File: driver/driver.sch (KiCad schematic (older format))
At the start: 13 parts, among them J1 BARREL_JACK, U1 MCP23017, U2 Teensy3.2, U3 MCP23017, U4 LM7815CT, U5 MCP23017, U6 LF50ABDT-TR, U7 MCP23017, U8 MCP23017, U9 MCP23017

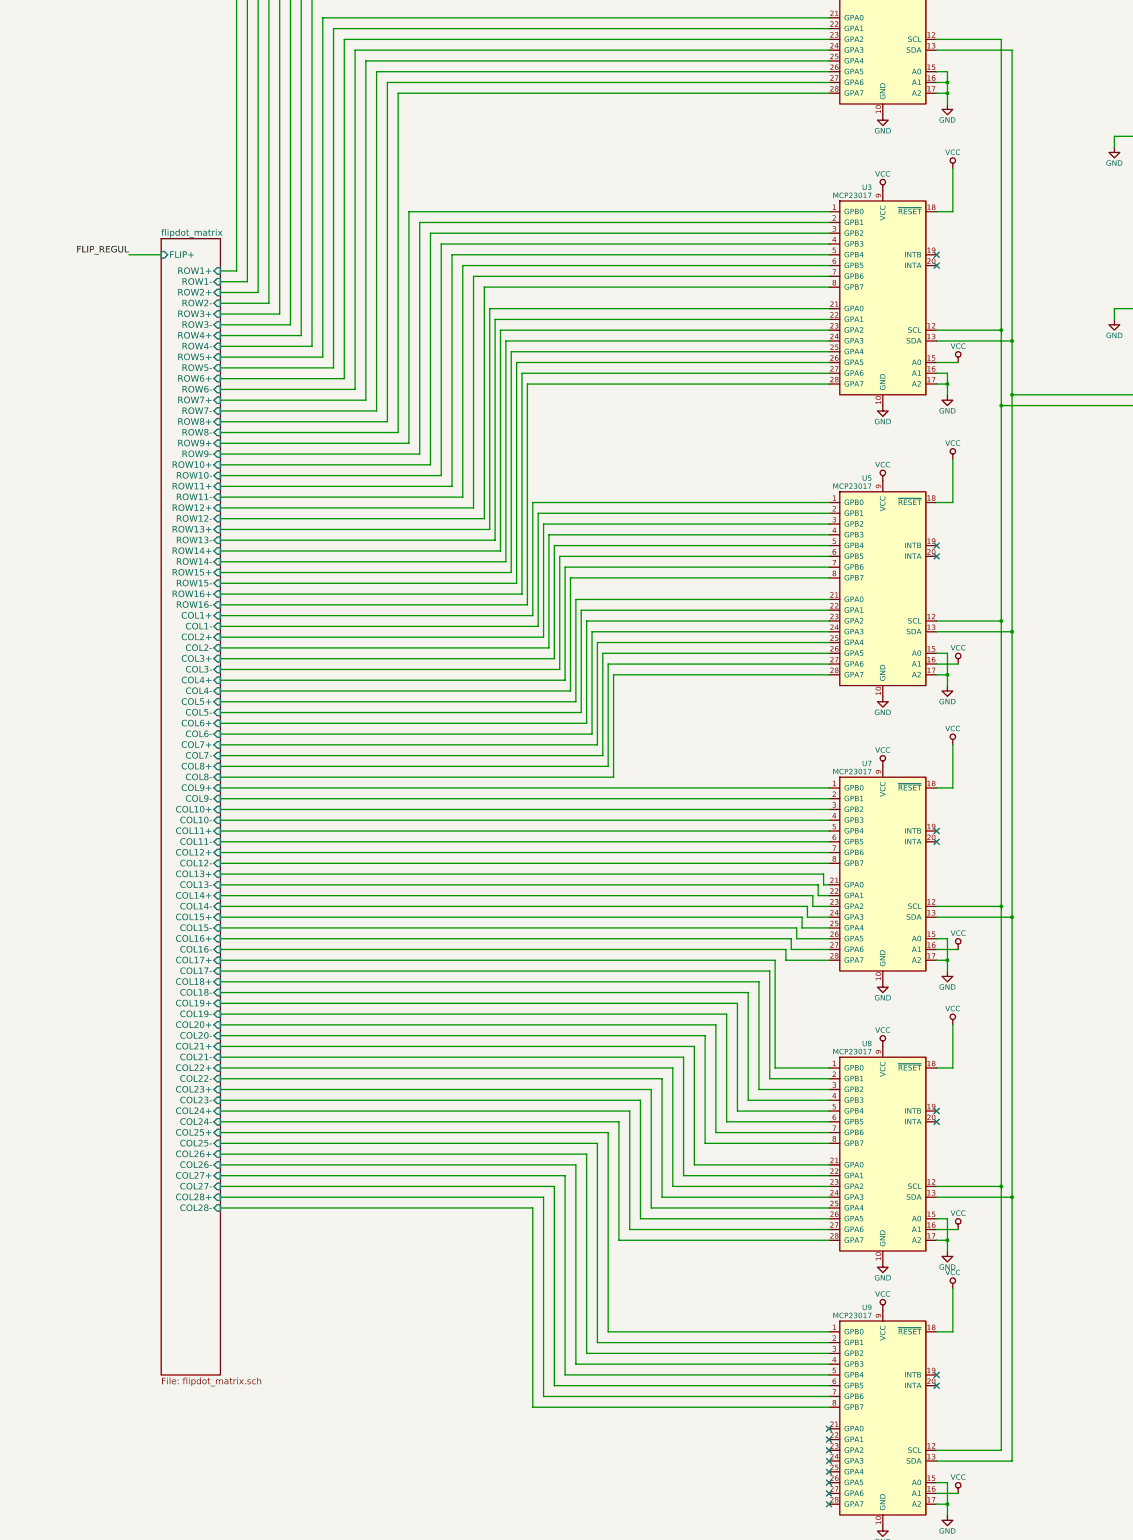
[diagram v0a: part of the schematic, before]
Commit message: Better row pins
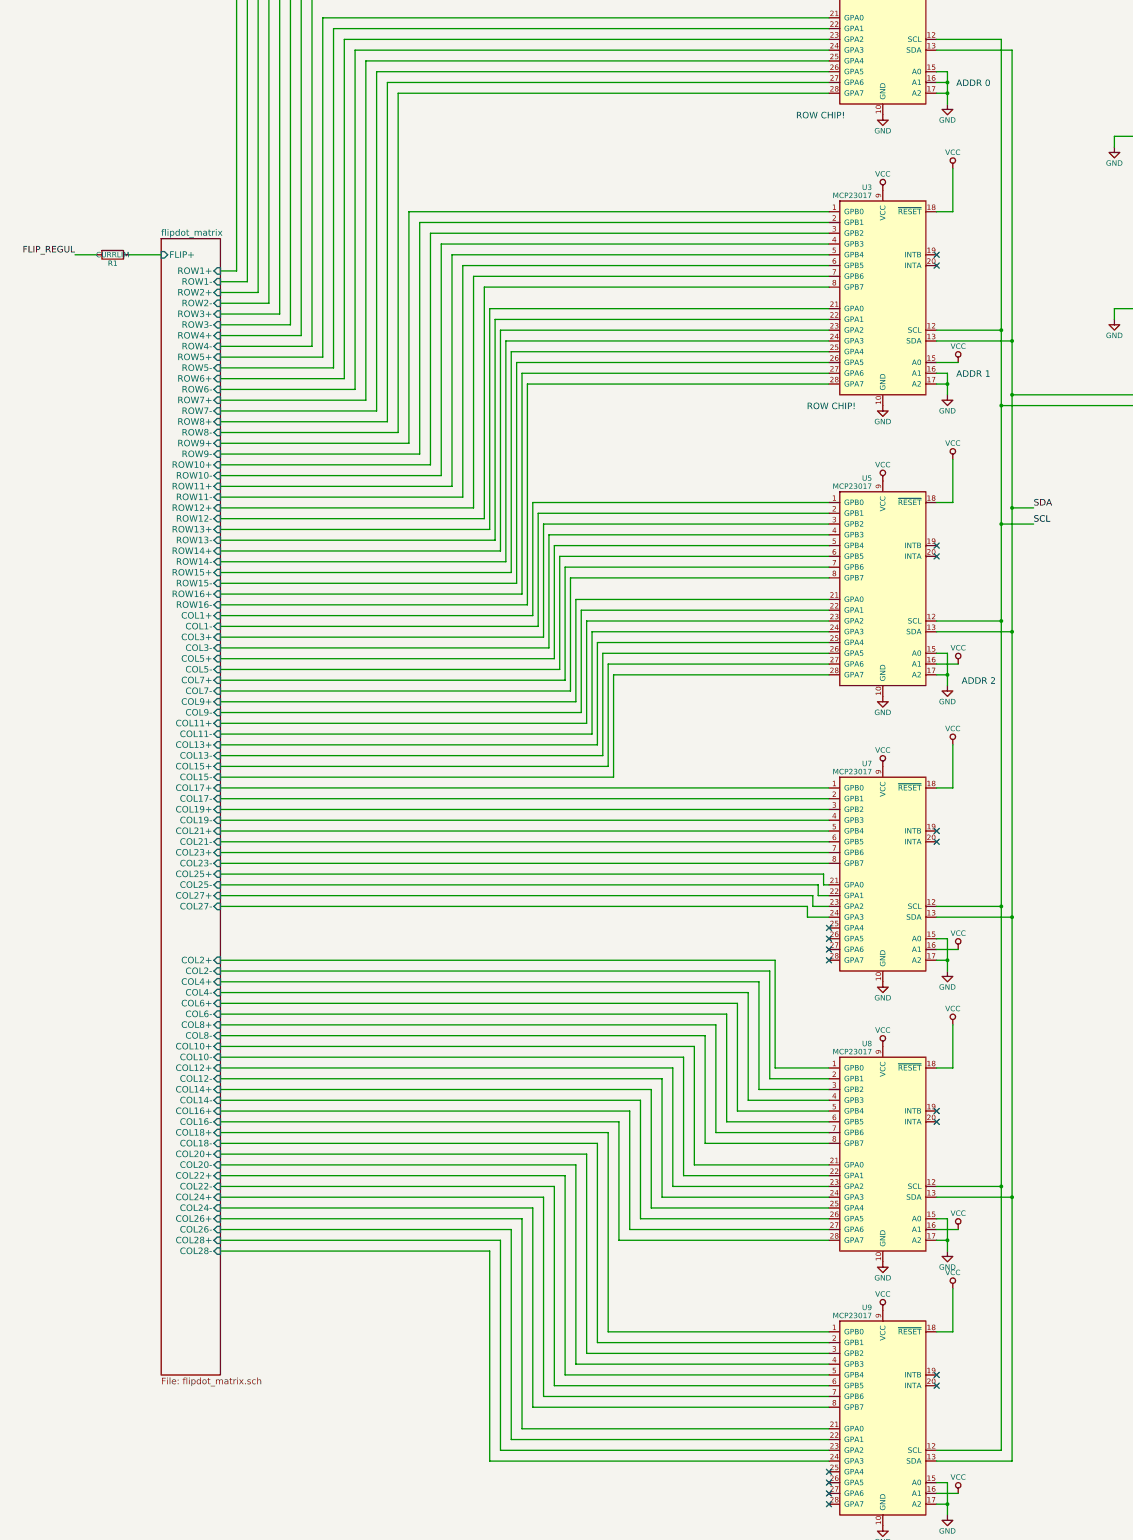
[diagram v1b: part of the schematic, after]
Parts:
- added R1: CURRLIM, symbol R
- C1, C2, C3: footprint (none) -> Capacitors_THT:CP_Radial_Tantal_D10.5mm_P5.00mm
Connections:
- net FLIP_REGUL: now also R1.2
- net flipdot_matrix/COL10+: now also U8.21 (GPA0); no longer U7.3 (GPB2)
- net flipdot_matrix/COL10-: now also U8.22 (GPA1); no longer U7.4 (GPB3)
- net flipdot_matrix/COL11+: now also U5.23 (GPA2); no longer U7.5 (GPB4)
- net flipdot_matrix/COL11-: now also U5.24 (GPA3); no longer U7.6 (GPB5)
- net flipdot_matrix/COL12+: now also U8.23 (GPA2); no longer U7.7 (GPB6)
- net flipdot_matrix/COL12-: now also U8.24 (GPA3); no longer U7.8 (GPB7)
- net flipdot_matrix/COL13+: now also U5.25 (GPA4); no longer U7.21 (GPA0)
- net flipdot_matrix/COL13-: now also U5.26 (GPA5); no longer U7.22 (GPA1)
- net flipdot_matrix/COL14+: now also U8.25 (GPA4); no longer U7.23 (GPA2)
- net flipdot_matrix/COL14-: now also U8.26 (GPA5); no longer U7.24 (GPA3)
- net flipdot_matrix/COL15+: now also U5.27 (GPA6); no longer U7.25 (GPA4)
- net flipdot_matrix/COL15-: now also U5.28 (GPA7); no longer U7.26 (GPA5)
- net flipdot_matrix/COL16+: now also U8.27 (GPA6); no longer U7.27 (GPA6)
- net flipdot_matrix/COL16-: now also U8.28 (GPA7); no longer U7.28 (GPA7)
- net flipdot_matrix/COL17+: now also U7.1 (GPB0); no longer U8.1 (GPB0)
- net flipdot_matrix/COL17-: now also U7.2 (GPB1); no longer U8.2 (GPB1)
- net flipdot_matrix/COL18+: now also U9.1 (GPB0); no longer U8.3 (GPB2)
- net flipdot_matrix/COL18-: now also U9.2 (GPB1); no longer U8.4 (GPB3)
- net flipdot_matrix/COL19+: now also U7.3 (GPB2); no longer U8.5 (GPB4)
- net flipdot_matrix/COL19-: now also U7.4 (GPB3); no longer U8.6 (GPB5)
- net flipdot_matrix/COL2+: now also U8.1 (GPB0); no longer U5.3 (GPB2)
- net flipdot_matrix/COL2-: now also U8.2 (GPB1); no longer U5.4 (GPB3)
- net flipdot_matrix/COL20+: now also U9.3 (GPB2); no longer U8.7 (GPB6)
- net flipdot_matrix/COL20-: now also U9.4 (GPB3); no longer U8.8 (GPB7)
- net flipdot_matrix/COL21+: now also U7.5 (GPB4); no longer U8.21 (GPA0)
- net flipdot_matrix/COL21-: now also U7.6 (GPB5); no longer U8.22 (GPA1)
- net flipdot_matrix/COL22+: now also U9.5 (GPB4); no longer U8.23 (GPA2)
- net flipdot_matrix/COL22-: now also U9.6 (GPB5); no longer U8.24 (GPA3)
- net flipdot_matrix/COL23+: now also U7.7 (GPB6); no longer U8.25 (GPA4)
- net flipdot_matrix/COL23-: now also U7.8 (GPB7); no longer U8.26 (GPA5)
- net flipdot_matrix/COL24+: now also U9.7 (GPB6); no longer U8.27 (GPA6)
- net flipdot_matrix/COL24-: now also U9.8 (GPB7); no longer U8.28 (GPA7)
- net flipdot_matrix/COL25+: now also U7.21 (GPA0); no longer U9.1 (GPB0)
- net flipdot_matrix/COL25-: now also U7.22 (GPA1); no longer U9.2 (GPB1)
- net flipdot_matrix/COL26+: now also U9.21 (GPA0); no longer U9.3 (GPB2)
- net flipdot_matrix/COL26-: now also U9.22 (GPA1); no longer U9.4 (GPB3)
- net flipdot_matrix/COL27+: now also U7.23 (GPA2); no longer U9.5 (GPB4)
- net flipdot_matrix/COL27-: now also U7.24 (GPA3); no longer U9.6 (GPB5)
- net flipdot_matrix/COL28+: now also U9.23 (GPA2); no longer U9.7 (GPB6)
- net flipdot_matrix/COL28-: now also U9.24 (GPA3); no longer U9.8 (GPB7)
- net flipdot_matrix/COL3+: now also U5.3 (GPB2); no longer U5.5 (GPB4)
- net flipdot_matrix/COL3-: now also U5.4 (GPB3); no longer U5.6 (GPB5)
- net flipdot_matrix/COL4+: now also U8.3 (GPB2); no longer U5.7 (GPB6)
- net flipdot_matrix/COL4-: now also U8.4 (GPB3); no longer U5.8 (GPB7)
- net flipdot_matrix/COL5+: now also U5.5 (GPB4); no longer U5.21 (GPA0)
- net flipdot_matrix/COL5-: now also U5.6 (GPB5); no longer U5.22 (GPA1)
- net flipdot_matrix/COL6+: now also U8.5 (GPB4); no longer U5.23 (GPA2)
- net flipdot_matrix/COL6-: now also U8.6 (GPB5); no longer U5.24 (GPA3)
- net flipdot_matrix/COL7+: now also U5.7 (GPB6); no longer U5.25 (GPA4)
- net flipdot_matrix/COL7-: now also U5.8 (GPB7); no longer U5.26 (GPA5)
- net flipdot_matrix/COL8+: now also U8.7 (GPB6); no longer U5.27 (GPA6)
- net flipdot_matrix/COL8-: now also U8.8 (GPB7); no longer U5.28 (GPA7)
- net flipdot_matrix/COL9+: now also U5.21 (GPA0); no longer U7.1 (GPB0)
- net flipdot_matrix/COL9-: now also U5.22 (GPA1); no longer U7.2 (GPB1)
- net SCL: now reaches U1.12 (SCL), U2.26 (19_A5_SCL0_Touch), U3.12 (SCL), U5.12 (SCL), U7.12 (SCL), U8.12 (SCL), U9.12 (SCL)
- net SDA: now reaches U1.13 (SDA), U2.25 (18_A4_SDA0_Touch), U3.13 (SDA), U5.13 (SDA), U7.13 (SDA), U8.13 (SDA), U9.13 (SDA)
- new net flipdot_matrix/FLIP+: R1.1
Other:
- note added: "ADDR 0\n"
- note added: "ADDR 1"
- note added: "ADDR 2"
- note added: "ROW CHIP!"
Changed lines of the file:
@@
 F35 "COL1+" I R 8050 7600 60
 F36 "COL1-" I R 8050 7700 60
-F37 "COL2+" I R 8050 7800 60
-F38 "COL2-" I R 8050 7900 60
-F39 "COL3+" I R 8050 8000 60
-F40 "COL4+" I R 8050 8200 60
-F41 "COL3-" I R 8050 8100 60
-F42 "COL4-" I R 8050 8300 60
-F43 "COL5-" I R 8050 8500 60
-F44 "COL5+" I R 8050 8400 60
-F45 "COL6+" I R 8050 8600 60
-F46 "COL6-" I R 8050 8700 60
-F47 "COL7-" I R 8050 8900 60
-F48 "COL7+" I R 8050 8800 60
-F49 "COL8-" I R 8050 9100 60
-F50 "COL8+" I R 8050 9000 60
-F51 "COL9+" I R 8050 9200 60
-F52 "COL9-" I R 8050 9300 60
-F53 "COL10-" I R 8050 9500 60
-F54 "COL11-" I R 8050 9700 60
-F55 "COL10+" I R 8050 9400 60
-F56 "COL11+" I R 8050 9600 60
-F57 "COL12+" I R 8050 9800 60
-F58 "COL12-" I R 8050 9900 60
-F59 "COL13+" I R 8050 10000 60
-F60 "COL14+" I R 8050 10200 60
-F61 "COL13-" I R 8050 10100 60
-F62 "COL14-" I R 8050 10300 60
-F63 "COL15+" I R 8050 10400 60
-F64 "COL15-" I R 8050 10500 60
-F65 "COL16+" I R 8050 10600 60
-F66 "COL16-" I R 8050 10700 60
-F67 "COL17+" I R 8050 10800 60
-F68 "COL18+" I R 8050 11000 60
-F69 "COL17-" I R 8050 10900 60
-F70 "COL18-" I R 8050 11100 60
-F71 "COL19-" I R 8050 11300 60
-F72 "COL19+" I R 8050 11200 60
-F73 "COL20+" I R 8050 11400 60
-F74 "COL20-" I R 8050 11500 60
-F75 "COL21-" I R 8050 11700 60
-F76 "COL21+" I R 8050 11600 60
-F77 "COL22-" I R 8050 11900 60
-F78 "COL22+" I R 8050 11800 60
-F79 "COL23+" I R 8050 12000 60
-F80 "COL23-" I R 8050 12100 60
-F81 "COL24-" I R 8050 12300 60
-F82 "COL25-" I R 8050 12500 60
-F83 "COL24+" I R 8050 12200 60
-F84 "COL25+" I R 8050 12400 60
-F85 "COL26+" I R 8050 12600 60
-F86 "COL26-" I R 8050 12700 60
-F87 "COL27+" I R 8050 12800 60
-F88 "COL28+" I R 8050 13000 60
-F89 "COL27-" I R 8050 12900 60
-F90 "COL28-" I R 8050 13100 60
+F37 "COL2+" I R 8050 10800 60
+F38 "COL2-" I R 8050 10900 60
+F39 "COL3+" I R 8050 7800 60
+F40 "COL4+" I R 8050 11000 60
+F41 "COL3-" I R 8050 7900 60
+F42 "COL4-" I R 8050 11100 60
+F43 "COL5-" I R 8050 8100 60
+F44 "COL5+" I R 8050 8000 60
+F45 "COL6+" I R 8050 11200 60
+F46 "COL6-" I R 8050 11300 60
+F47 "COL7-" I R 8050 8300 60
+F48 "COL7+" I R 8050 8200 60
+F49 "COL8-" I R 8050 11500 60
+F50 "COL8+" I R 8050 11400 60
+F51 "COL9+" I R 8050 8400 60
+F52 "COL9-" I R 8050 8500 60
+F53 "COL10-" I R 8050 11700 60
+F54 "COL11-" I R 8050 8700 60
+F55 "COL10+" I R 8050 11600 60
+F56 "COL11+" I R 8050 8600 60
+F57 "COL12+" I R 8050 11800 60
+F58 "COL12-" I R 8050 11900 60
+F59 "COL13+" I R 8050 8800 60
+F60 "COL14+" I R 8050 12000 60
+F61 "COL13-" I R 8050 8900 60
+F62 "COL14-" I R 8050 12100 60
+F63 "COL15+" I R 8050 9000 60
+F64 "COL15-" I R 8050 9100 60
+F65 "COL16+" I R 8050 12200 60
+F66 "COL16-" I R 8050 12300 60
+F67 "COL17+" I R 8050 9200 60
+F68 "COL18+" I R 8050 12400 60
+F69 "COL17-" I R 8050 9300 60
+F70 "COL18-" I R 8050 12500 60
+F71 "COL19-" I R 8050 9500 60
+F72 "COL19+" I R 8050 9400 60
+F73 "COL20+" I R 8050 12600 60
+F74 "COL20-" I R 8050 12700 60
+F75 "COL21-" I R 8050 9700 60
+F76 "COL21+" I R 8050 9600 60
+F77 "COL22-" I R 8050 12900 60
+F78 "COL22+" I R 8050 12800 60
+F79 "COL23+" I R 8050 9800 60
+F80 "COL23-" I R 8050 9900 60
+F81 "COL24-" I R 8050 13100 60
+F82 "COL25-" I R 8050 10100 60
+F83 "COL24+" I R 8050 13000 60
+F84 "COL25+" I R 8050 10000 60
+F85 "COL26+" I R 8050 13200 60
+F86 "COL26-" I R 8050 13300 60
+F87 "COL27+" I R 8050 10200 60
+F88 "COL28+" I R 8050 13400 60
+F89 "COL27-" I R 8050 10300 60
+F90 "COL28-" I R 8050 13500 60
 $EndSheet
 Wire Wire Line
@@
 	13500 10300 8050 10300
 Wire Wire Line
-	13700 10500 13450 10500
-Wire Wire Line
-	13450 10500 13450 10400
-Wire Wire Line
-	13450 10400 8050 10400
-Wire Wire Line
-	13700 10600 13400 10600
-Wire Wire Line
-	13400 10600 13400 10500
-Wire Wire Line
-	13400 10500 8050 10500
-Wire Wire Line
-	13700 10700 13350 10700
-Wire Wire Line
-	13350 10700 13350 10600
-Wire Wire Line
-	13350 10600 8050 10600
-Wire Wire Line
-	13700 10800 13300 10800
-Wire Wire Line
-	13300 10800 13300 10700
-Wire Wire Line
-	13300 10700 8050 10700
-Wire Wire Line
 	13700 11800 13200 11800
 Wire Wire Line
@@
 Wire Wire Line
 	8050 13100 10950 13100
-NoConn ~ 13700 15150
-NoConn ~ 13700 15250
-NoConn ~ 13700 15350
-NoConn ~ 13700 15450
 NoConn ~ 13700 15550
 NoConn ~ 13700 15650
@@
 Wire Wire Line
 	7500 4250 7200 4250
-Text Label 7200 4250 2    60   ~ 0
+Text Label 6700 4250 2    60   ~ 0
 FLIP_REGUL
 Wire Wire Line
@@
 F 0 "C1" H 19175 8000 50  0000 L CNN
 F 1 "10uF" H 19175 7800 50  0000 L CNN
-F 2 "" H 19188 7750 50  0001 C CNN
+F 2 "Capacitors_THT:CP_Radial_Tantal_D10.5mm_P5.00mm" H 19188 7750 50  0001 C CNN
 F 3 "" H 19150 7900 50  0001 C CNN
 	1    19150 7900
@@
 F 0 "C2" H 20575 8000 50  0000 L CNN
 F 1 "10uF" H 20575 7800 50  0000 L CNN
-F 2 "" H 20588 7750 50  0001 C CNN
+F 2 "Capacitors_THT:CP_Radial_Tantal_D10.5mm_P5.00mm" H 20588 7750 50  0001 C CNN
 F 3 "" H 20550 7900 50  0001 C CNN
 	1    20550 7900
@@
 F 0 "C3" H 19625 6750 50  0000 L CNN
 F 1 "10uF" H 19625 6550 50  0000 L CNN
-F 2 "" H 19638 6500 50  0001 C CNN
+F 2 "Capacitors_THT:CP_Radial_Tantal_D10.5mm_P5.00mm" H 19638 6500 50  0001 C CNN
 F 3 "" H 19600 6650 50  0001 C CNN
 	1    19600 6650
@@
 	1    0    0    -1
 $EndComp
+$Comp
+L R R1
+U 1 1 599924E8
+P 7050 4250
+F 0 "R1" V 7130 4250 50  0000 C CNN
+F 1 "CURRLIM" V 7050 4250 50  0000 C CNN
+F 2 "" V 6980 4250 50  0001 C CNN
+F 3 "" H 7050 4250 50  0001 C CNN
+	1    7050 4250
+	0    1    1    0
+$EndComp
+Wire Wire Line
+	6700 4250 6900 4250
+Text Notes 15200 2700 2    60   ~ 0
+ADDR 0\n
+Text Notes 15200 5400 2    60   ~ 0
+ADDR 1
+Text Notes 15250 8250 2    60   ~ 0
+ADDR 2
+Wire Wire Line
+	15400 6600 15600 6600
+Connection ~ 15400 6600
+Wire Wire Line
+	15300 6750 15600 6750
+Connection ~ 15300 6750
+Text Label 15600 6600 0    60   ~ 0
+SDA
+Text Label 15600 6750 0    60   ~ 0
+SCL
+Text Notes 13850 3000 2    60   ~ 0
+ROW CHIP!
+Text Notes 13950 5700 2    60   ~ 0
+ROW CHIP!
+NoConn ~ 13700 10500
+NoConn ~ 13700 10600
+NoConn ~ 13700 10700
+NoConn ~ 13700 10800
+Wire Wire Line
+	8050 13200 10850 13200
+Wire Wire Line
+	10850 13200 10850 15150
+Wire Wire Line
+	10850 15150 13700 15150
+Wire Wire Line
+	13700 15250 10750 15250
+Wire Wire Line
+	10750 15250 10750 13300
+Wire Wire Line
+	10750 13300 8050 13300
+Wire Wire Line
+	8050 13400 10650 13400
+Wire Wire Line
+	10650 13400 10650 15350
+Wire Wire Line
+	10650 15350 13700 15350
+Wire Wire Line
+	13700 15450 10550 15450
+Wire Wire Line
+	10550 15450 10550 13500
+Wire Wire Line
+	10550 13500 8050 13500
 $EndSCHEMATC
